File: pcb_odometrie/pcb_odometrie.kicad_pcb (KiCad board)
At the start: 4 copper layers, 44.5 x 56 mm, 43 parts, among them J1 USB_C_Receptacle_USB2.0_16P, J10 Conn_01x06, J11 Conn_01x06, J12 Conn_01x06, J13 Conn_01x06, J2 Conn_ST_STDC14, J3 1755736, J4 Conn_02x06_Row_Letter_First, J5 Conn_02x04_Row_Letter_First, J6 Conn_01x06, J7 Conn_01x06, J8 Conn_01x06, J9 Conn_01x06, U1 STM32G491KEU6, U2 MCP23017T-E/SO

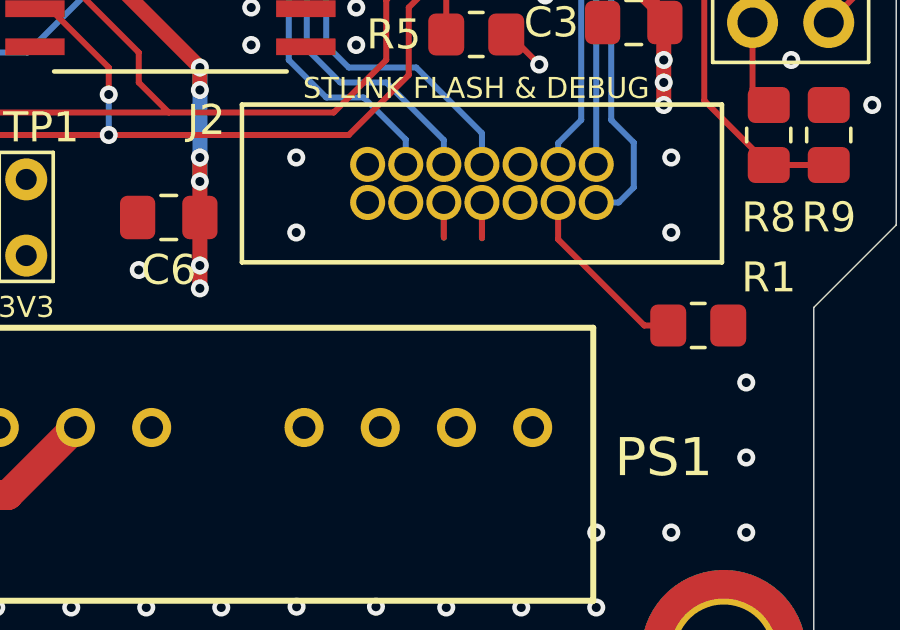
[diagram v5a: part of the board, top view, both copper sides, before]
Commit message: Ajout BAU servo PAMI, finitions PCB Actionneurs, fichier fab stencil. Version commandée PAMI & Actionneurs
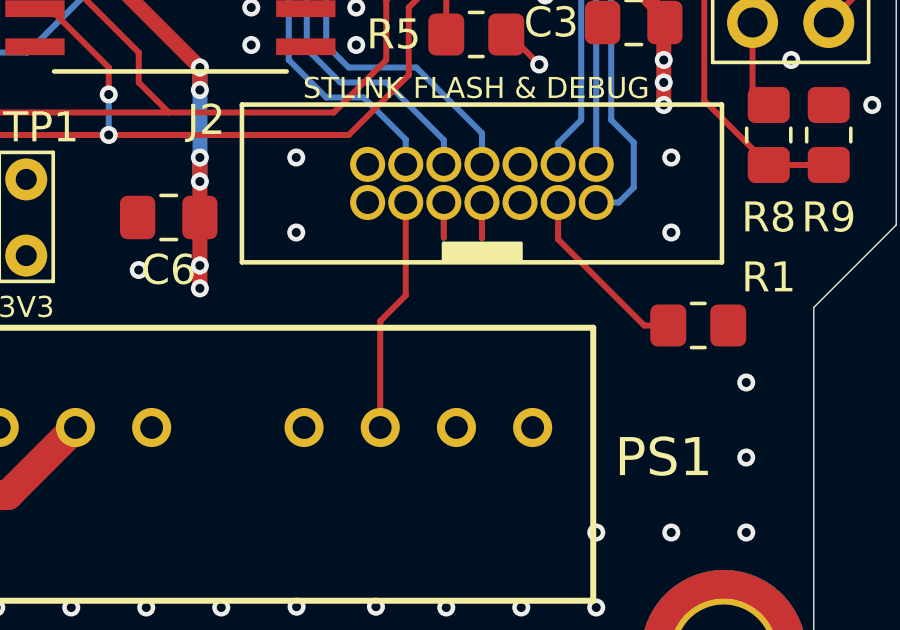
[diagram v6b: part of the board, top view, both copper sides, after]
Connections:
- J4 pad a3: /IN1A -> /IN1B
- J4 pad a4: /IN2A -> /IN2B
- J4 pad a5: /ENA -> /ENB
- J4 pad a6: /CTA -> /CTB
- J4 pad b3: /IN1B -> /IN1A
- J4 pad b4: /IN2B -> /IN2A
- J4 pad b5: /ENB -> /ENA
- J4 pad b6: /CTB -> /CTA
- R10 pad 2: /CTB -> /CTA
- R4 pad 2: /IN2B -> /IN2A
- R8 pad 1: /CTA -> /CTB
- U1 pad 13: /ENB -> /ENA
- U1 pad 18: /IN1A -> /IN1B
- U1 pad 19: /IN2A -> /IN2B
- U1 pad 20: /ENA -> /ENB
- U1 pad 29: /IN1B -> /IN1A
- U1 pad 31: /IN2B -> /IN2A
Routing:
- net /IN2B: track 32.6 -> 13.4 mm
- net /IN2A: track 13.4 -> 32.6 mm
- net /CTB: track 17.1 -> 2.97 mm
- net /CTA: track 2.97 -> 17.1 mm
- net +3V3: track 71.3 -> 79.1 mm
- net /ENB: track 19.5 -> 15.3 mm
- net /ENA: track 15.3 -> 19.5 mm
- net /IN1B: track 14.5 -> 12.4 mm
- net /IN1A: track 12.4 -> 14.5 mm
